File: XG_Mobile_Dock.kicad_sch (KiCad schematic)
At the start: 23 parts, among them J1 5-1775443-8, J13 Conn_01x06, J17 8730, J2 20455-040E-76, J3 20455-040E-76, J4 3-2362375-4, J7 Conn_02x10_Odd_Even, J8 Conn_02x10_Odd_Even, SW1 SW_Push

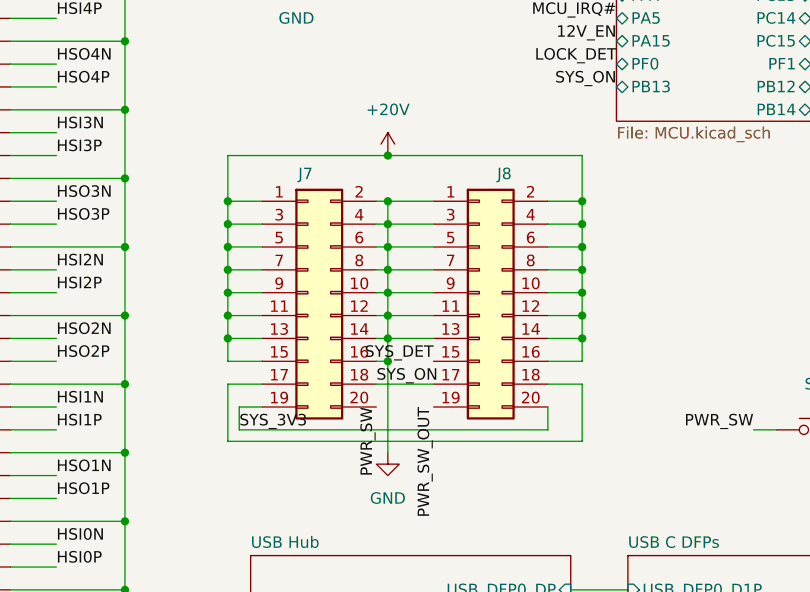
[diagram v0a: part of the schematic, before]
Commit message: pcb: move 20P crossover to cable
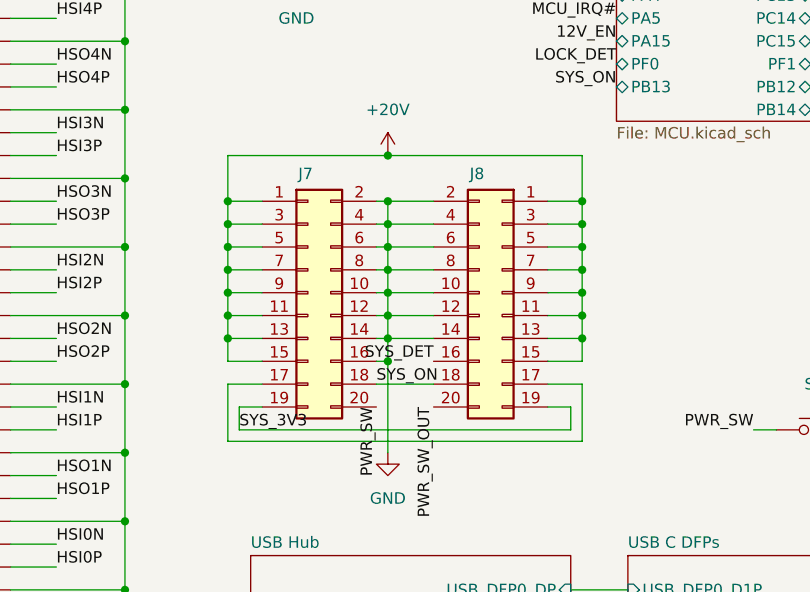
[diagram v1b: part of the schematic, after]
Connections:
- net +20V: now also J8.1 (Pin_1), J8.11 (Pin_11), J8.13 (Pin_13), J8.15 (Pin_15), J8.3 (Pin_3), J8.5 (Pin_5), J8.7 (Pin_7), J8.9 (Pin_9); no longer J8.10 (Pin_10), J8.12 (Pin_12), J8.14 (Pin_14), J8.16 (Pin_16), J8.2 (Pin_2), J8.4 (Pin_4), J8.6 (Pin_6), J8.8 (Pin_8)
- net GND: now also J8.10 (Pin_10), J8.12 (Pin_12), J8.14 (Pin_14), J8.2 (Pin_2), J8.4 (Pin_4), J8.6 (Pin_6), J8.8 (Pin_8); no longer J8.1 (Pin_1), J8.11 (Pin_11), J8.13 (Pin_13), J8.3 (Pin_3), J8.5 (Pin_5), J8.7 (Pin_7), J8.9 (Pin_9)
- net PWR_SW_OUT: now also J8.20 (Pin_20); no longer J8.19 (Pin_19)
- net SYS_3V3: now also J8.19 (Pin_19); no longer J8.20 (Pin_20)
- net SYS_DET: now also J8.16 (Pin_16); no longer J8.15 (Pin_15)
- net SYS_ON: now also J8.18 (Pin_18); no longer J8.17 (Pin_17)
- net at J7.17 (Pin_17): now also J8.17 (Pin_17); no longer J8.18 (Pin_18)

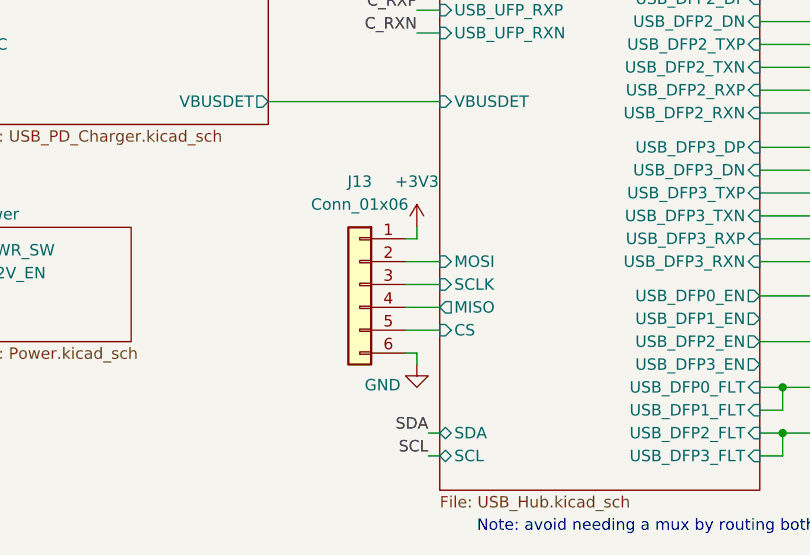
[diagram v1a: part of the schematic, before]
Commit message: pcb: connect SPI flash to VIA IC
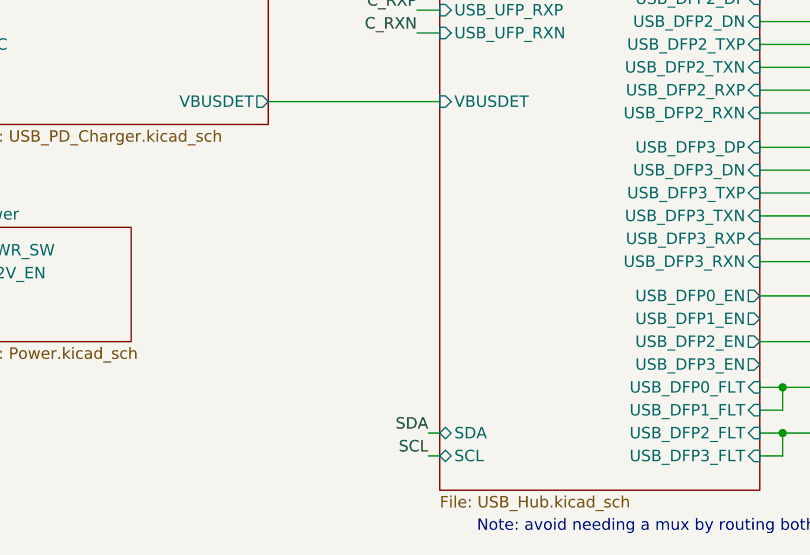
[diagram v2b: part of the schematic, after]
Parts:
- removed J13: Conn_01x06, Connector_PinHeader_2.54mm:PinHeader_1x06_P2.54mm_Vertical, symbol Connector_Generic:Conn_01x06
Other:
- sheet USB Hub ports: added none; removed CS, MISO, MOSI, SCLK

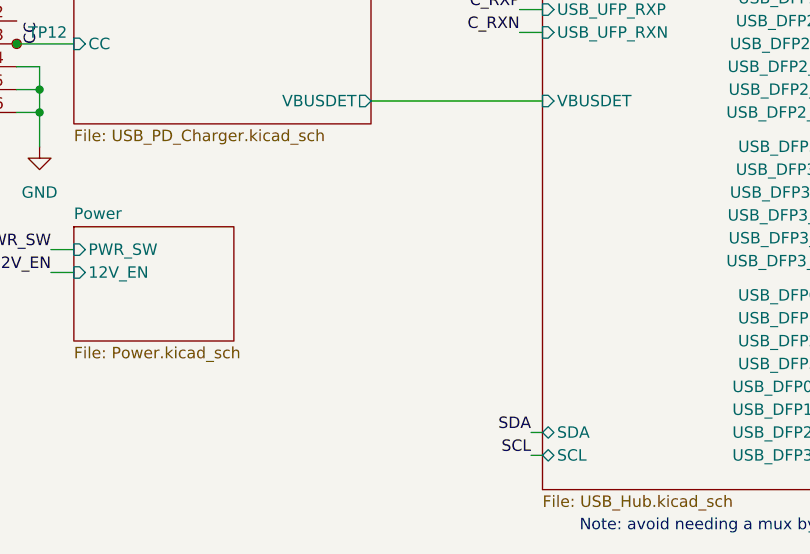
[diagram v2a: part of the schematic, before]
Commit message: pcb: add 12V PCIe power converters
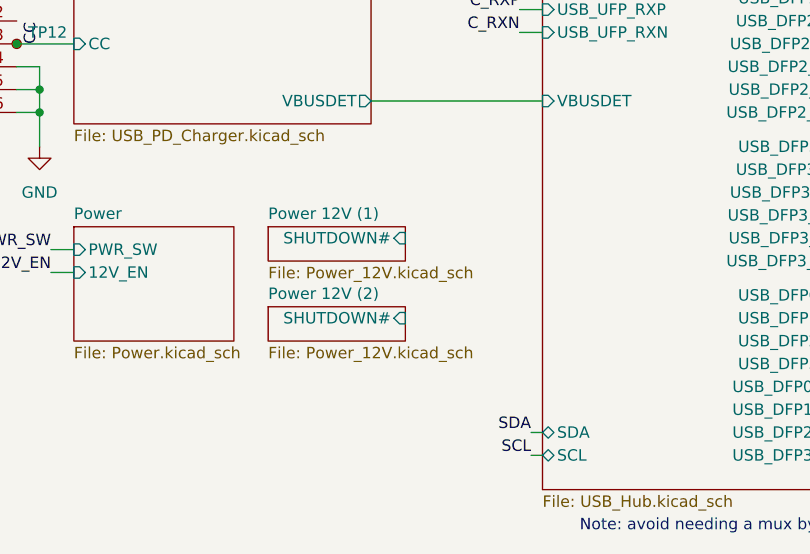
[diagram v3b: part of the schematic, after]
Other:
- added sheet Power 12V (1) (Power_12V.kicad_sch)
- added sheet Power 12V (2) (Power_12V.kicad_sch)
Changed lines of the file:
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@@
+	)
+	(sheet
+		(at 66.04 166.37)
+		(size 15.24 3.81)
+		(fields_autoplaced yes)
+		(stroke
+			(width 0.1524)
+			(type solid)
+		)
+		(fill
+			(color 0 0 0 0.0000)
+		)
+		(property "Sheetname" "Power 12V (1)"
+			(at 66.04 165.6584 0)
+			(effects
+				(font
+					(size 1.27 1.27)
+				)
+				(justify left bottom)
+			)
+		)
+		(property "Sheetfile" "Power_12V.kicad_sch"
+			(at 66.04 170.7646 0)
+			(effects
+				(font
+					(size 1.27 1.27)
+				)
+				(justify left top)
+			)
+		)
+		(pin "SHUTDOWN#" input
+			(at 81.28 167.64 0)
+			(effects
+				(font
+					(size 1.27 1.27)
+				)
+				(justify right)
+			)
+		)
+		(instances
+			(project "XG_Mobile_Dock"
+				(path "/f97e6956-ab08-42cb-8fed-03fa58e87f0e"
+					(page "7")
+				)
+			)
+		)
+	)
+	(sheet
+		(at 66.04 175.26)
+		(size 15.24 3.81)
+		(fields_autoplaced yes)
+		(stroke
+			(width 0.1524)
+			(type solid)
+		)
+		(fill
+			(color 0 0 0 0.0000)
+		)
+		(property "Sheetname" "Power 12V (2)"
+			(at 66.04 174.5484 0)
+			(effects
+				(font
+					(size 1.27 1.27)
+				)
+				(justify left bottom)
+			)
+		)
+		(property "Sheetfile" "Power_12V.kicad_sch"
+			(at 66.04 179.6546 0)
+			(effects
+				(font
+					(size 1.27 1.27)
+				)
+				(justify left top)
+			)
+		)
+		(pin "SHUTDOWN#" input
+			(at 81.28 176.53 0)
+			(effects
+				(font
+					(size 1.27 1.27)
+				)
+				(justify right)
+			)
+		)
+		(instances
+			(project "XG_Mobile_Dock"
+				(path "/f97e6956-ab08-42cb-8fed-03fa58e87f0e"
+					(page "8")
+				)
+			)
+		)
 	)
 	(sheet
@@
 			(project "XG_Mobile_Dock"
 				(path "/f97e6956-ab08-42cb-8fed-03fa58e87f0e"
-					(page "7")
-				)
-			)
+					(page "9")
+				)
+			)

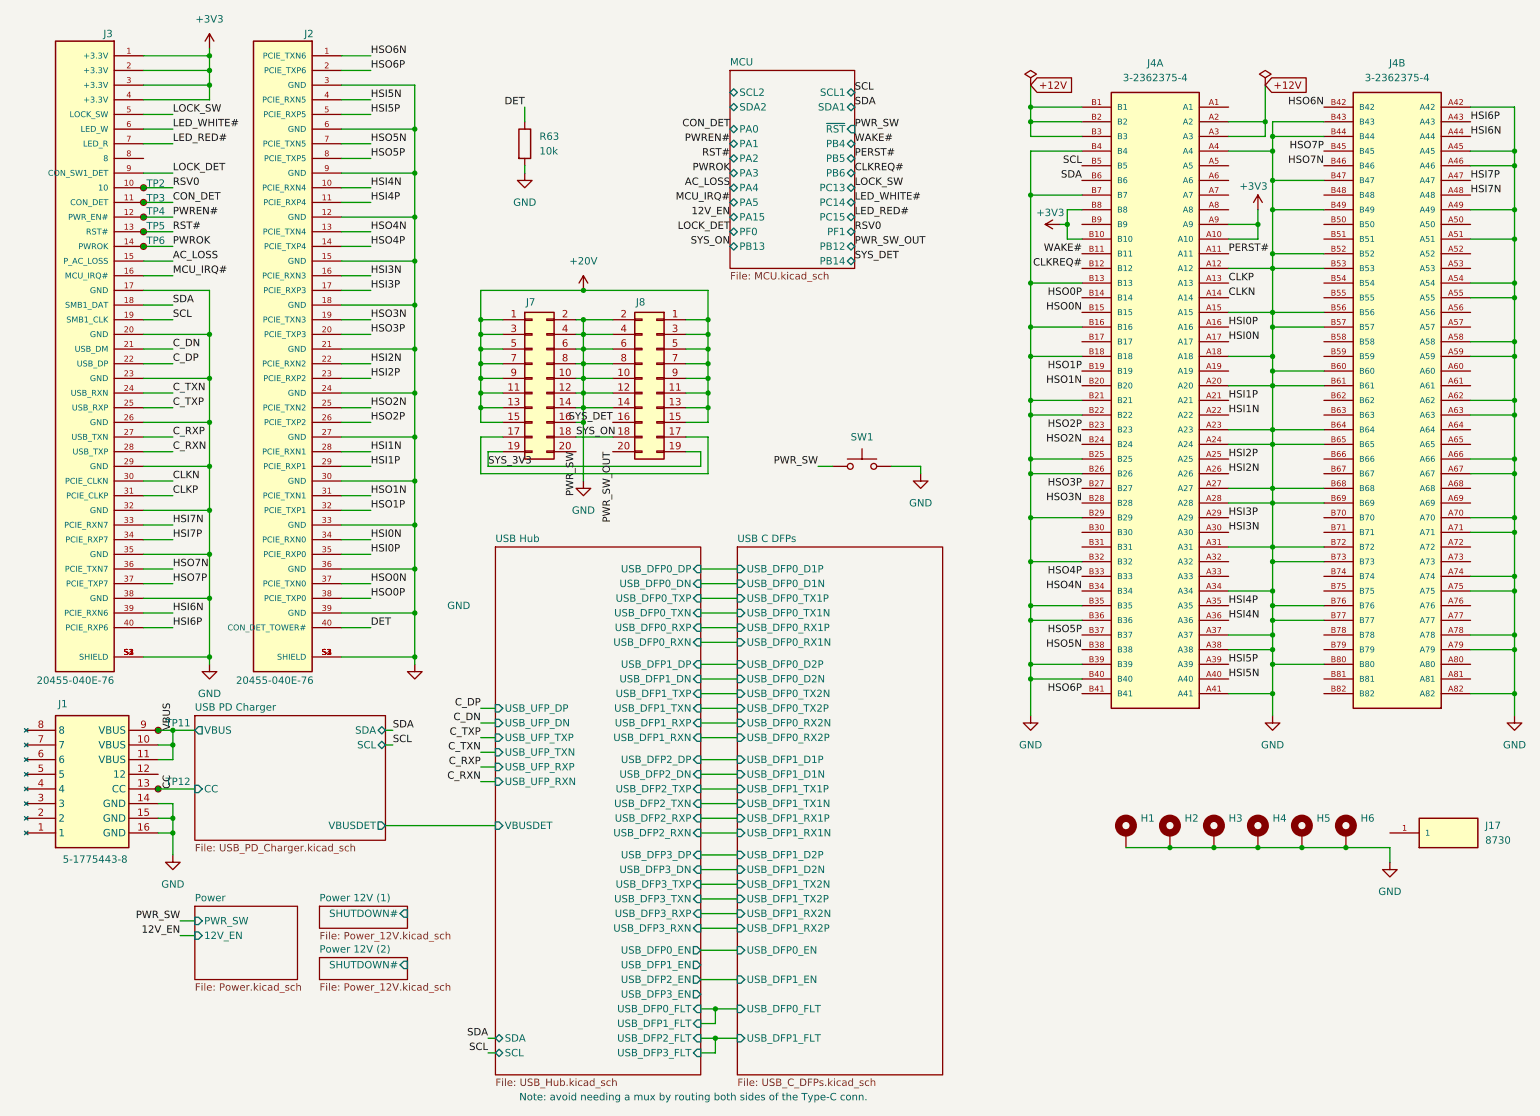
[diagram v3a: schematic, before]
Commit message: pcb: added fans and thermistor to standard pcb
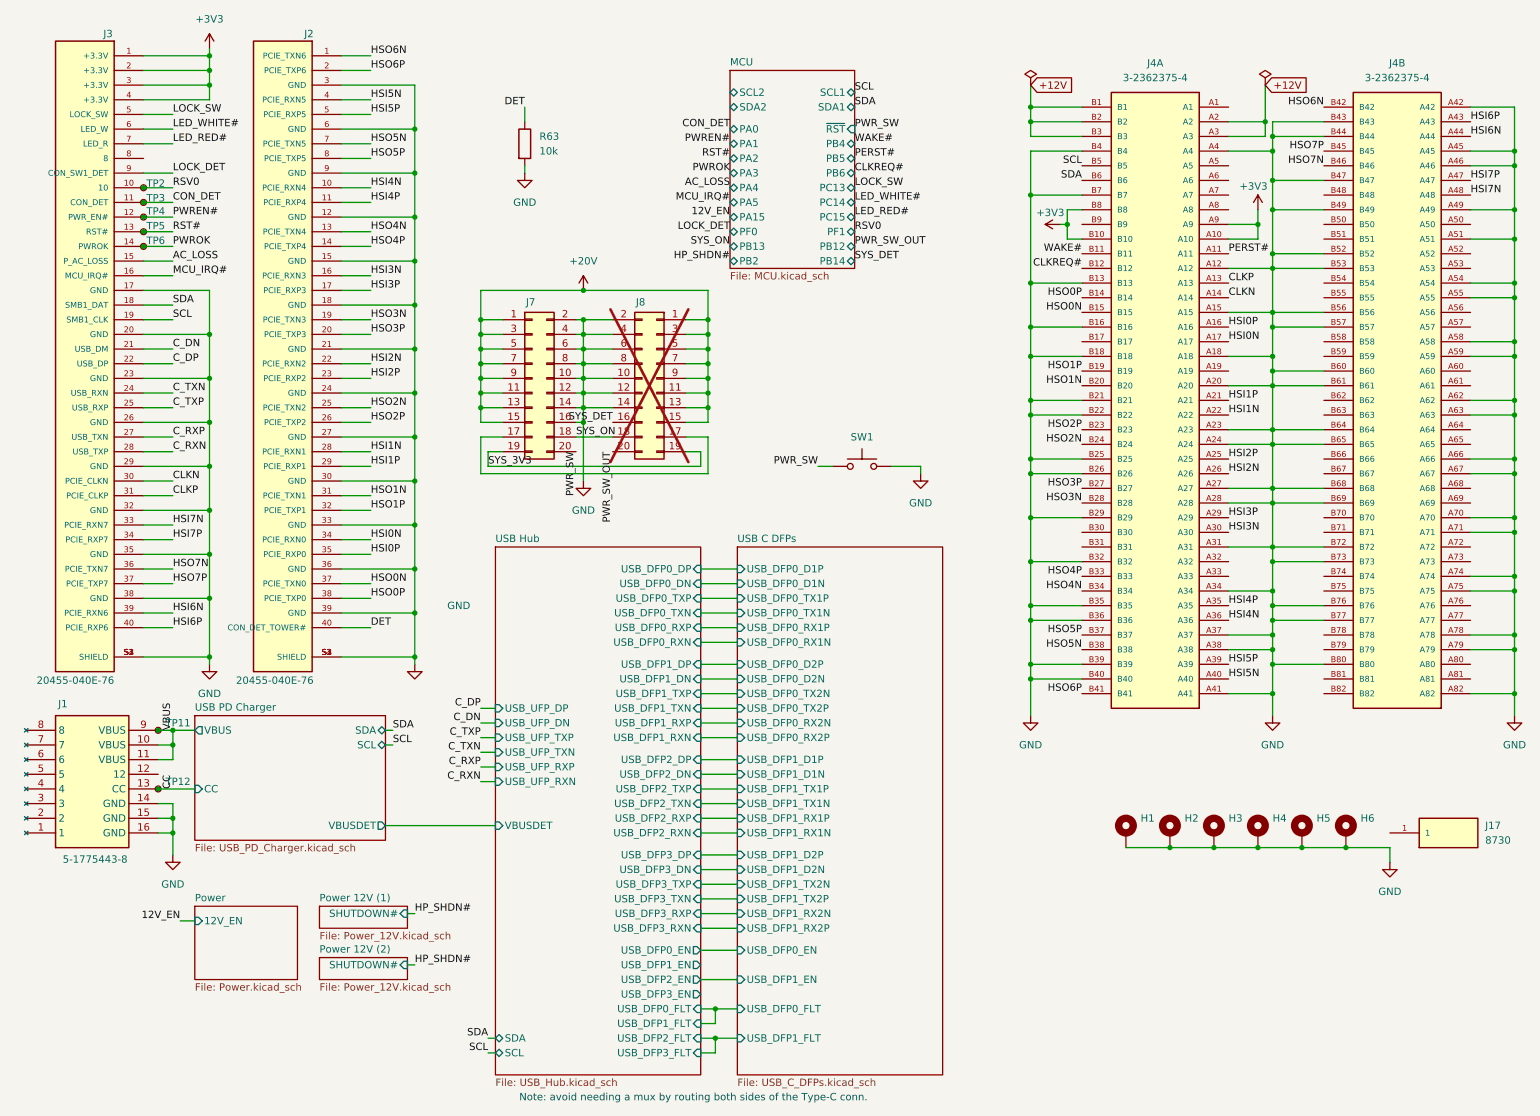
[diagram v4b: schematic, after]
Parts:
- J8: now not fitted; now left out of the parts list
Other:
- sheet MCU ports: added PB2; removed none
- sheet Power ports: added none; removed PWR_SW
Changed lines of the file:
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@@
 	(wire
 		(pts
+			(xy 81.28 167.64) (xy 82.55 167.64)
+		)
+		(stroke
+			(width 0)
+			(type default)
+		)
+	)
+	(wire
+		(pts
 			(xy 95.25 191.77) (xy 96.52 191.77)
 		)
@@
 	(wire
 		(pts
-			(xy 41.91 168.91) (xy 44.45 168.91)
-		)
-		(stroke
-			(width 0)
-			(type default)
-		)
-	)
-	(wire
-		(pts
 			(xy 93.98 64.77) (xy 93.98 59.69)
 		)
@@
 	(wire
 		(pts
-			(xy 41.91 171.45) (xy 44.45 171.45)
-		)
-		(stroke
-			(width 0)
-			(type default)
-		)
-	)
-	(wire
-		(pts
 			(xy 132.08 157.48) (xy 138.43 157.48)
 		)
@@
 	(wire
 		(pts
+			(xy 81.28 176.53) (xy 82.55 176.53)
+		)
+		(stroke
+			(width 0)
+			(type default)
+		)
+	)
+	(wire
+		(pts
 			(xy 132.08 118.11) (xy 138.43 118.11)
 		)
@@
 	(wire
 		(pts
+			(xy 41.91 168.91) (xy 44.45 168.91)
+		)
+		(stroke
+			(width 0)
+			(type default)
+		)
+	)
+	(wire
+		(pts
 			(xy 46.99 59.69) (xy 46.99 67.31)
 		)
@@
 		)
 	)
+	(label "HP_SHDN#"
+		(at 82.55 176.53 0)
+		(fields_autoplaced yes)
+		(effects
+			(font
+				(size 1.27 1.27)
+			)
+			(justify left bottom)
+		)
+	)
 	(label "PWROK"
 		(at 137.16 39.37 180)
@@
 	)
 	(label "12V_EN"
-		(at 41.91 171.45 180)
+		(at 41.91 168.91 180)
 		(fields_autoplaced yes)
 		(effects
@@
 		)
 	)
+	(label "HP_SHDN#"
+		(at 82.55 167.64 0)
+		(fields_autoplaced yes)
+		(effects
+			(font
+				(size 1.27 1.27)
+			)
+			(justify left bottom)
+		)
+	)
 	(label "HSI4N"
 		(at 74.93 41.91 0)
@@
 		)
 	)
-	(label "PWR_SW"
-		(at 41.91 168.91 180)
-		(fields_autoplaced yes)
-		(effects
-			(font
-				(size 1.27 1.27)
-			)
-			(justify right bottom)
-		)
-	)
 	(label "HSO2N"
 		(at 198.12 86.36 180)
@@
 		)
 	)
+	(label "HP_SHDN#"
+		(at 137.16 54.61 180)
+		(fields_autoplaced yes)
+		(effects
+			(font
+				(size 1.27 1.27)
+			)
+			(justify right bottom)
+		)
+	)
 	(label "C_TXP"
 		(at 93.98 137.16 180)
@@
 		(unit 1)
 		(exclude_from_sim no)
-		(in_bom yes)
+		(in_bom no)
 		(on_board yes)
-		(dnp no)
+		(dnp yes)
 		(property "Reference" "J8"
 			(at 121.666 61.722 0)
@@
 			)
 		)
-		(pin "PWR_SW" input
-			(at 44.45 168.91 180)
-			(effects
-				(font
-					(size 1.27 1.27)
-				)
-				(justify left)
-			)
-		)
 		(pin "12V_EN" input
-			(at 44.45 171.45 180)
+			(at 44.45 168.91 180)
 			(effects
 				(font
@@
 			(effects
 				(font
+					(size 1.27 1.27)
+				)
+				(justify left)
+			)
+		)
+		(pin "PB2" bidirectional
+			(at 137.16 54.61 180)
+			(effects
+				(font

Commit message: pcb: reduced gate resistor in schematic review
Also updated some missing attributes.
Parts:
- J1: LCSC (none) -> C17475182
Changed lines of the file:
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@@
+			)
+		)
+		(property "LCSC" "C17475182"
+			(at 15.24 153.67 0)
+			(effects
+				(font
+					(size 1.27 1.27)
+				)
+				(hide yes)
 			)
 		)

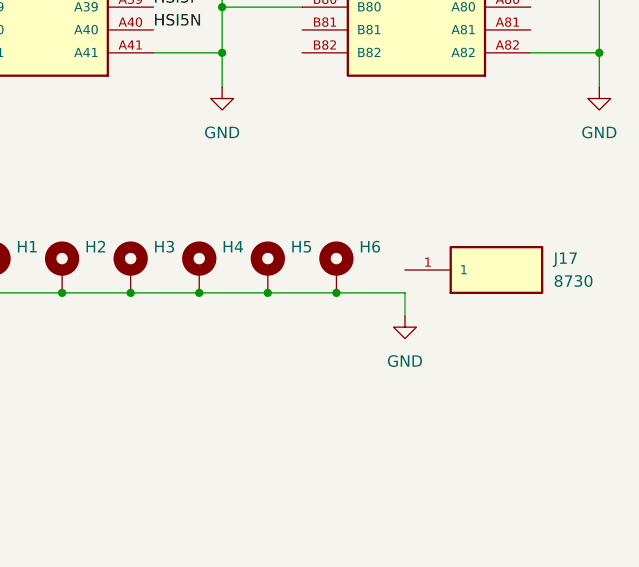
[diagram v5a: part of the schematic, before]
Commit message: pcb: restore gnd connection to mounting screw
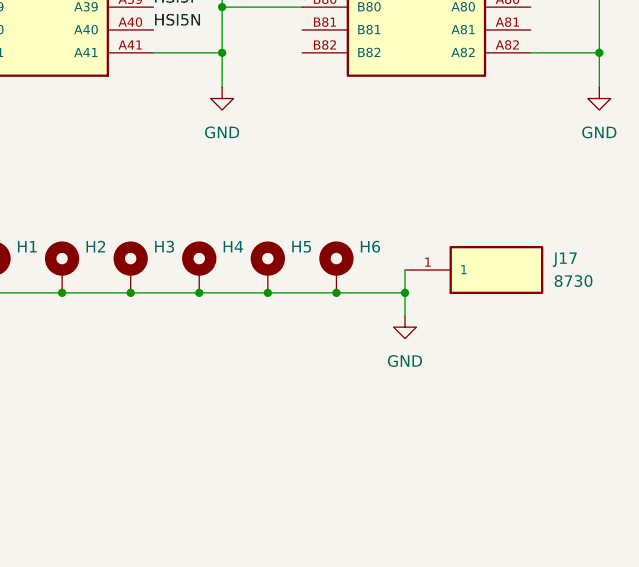
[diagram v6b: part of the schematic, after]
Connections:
- net GND: now also J17.1
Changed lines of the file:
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@@
 	)
 	(junction
+		(at 251.46 156.21)
+		(diameter 0)
+		(color 0 0 0 0)
+	)
+	(junction
 		(at 273.05 68.58)
 		(diameter 0)
@@
 		)
 		(stroke
+			(width 0)
+			(type default)
+		)
+	)
+	(wire
+		(pts
+			(xy 251.46 153.67) (xy 251.46 156.21)
+		)
+		(stroke
